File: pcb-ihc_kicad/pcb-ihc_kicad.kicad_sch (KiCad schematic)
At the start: 76 parts, among them J1 D-IN with pullup, J10 D-IN with pulldown, J11 2x N-Mosfet, J2 Screw_Terminal_01x01, J3 Screw_Terminal_01x01, J4 Screw_Terminal_01x01, J5 Screw_Terminal_01x01, J6 Screw_Terminal_01x01, J7 Screw_Terminal_01x01, J8 Screw_Terminal_01x01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

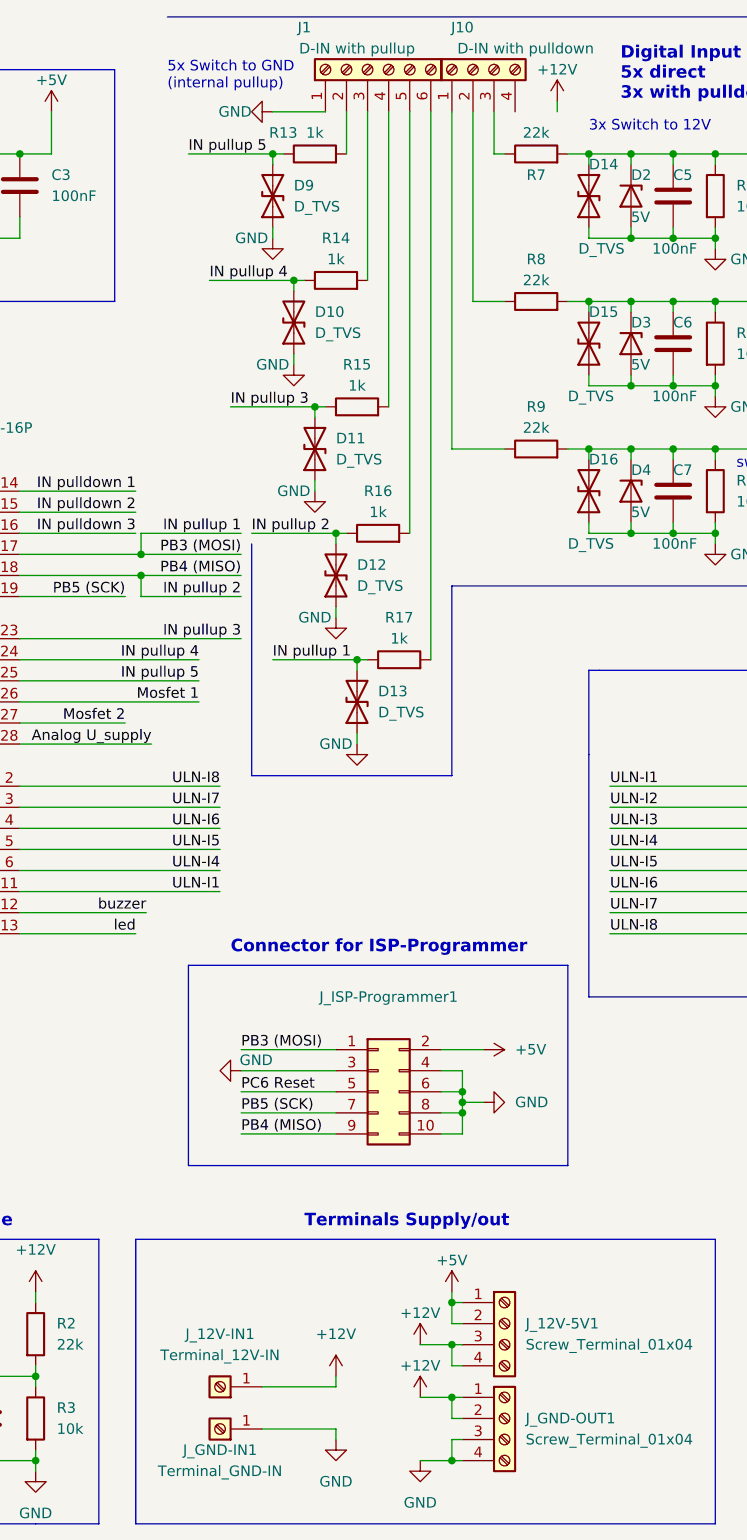
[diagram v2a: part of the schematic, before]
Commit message: Optimize routing and layout
- fix track width on several locations (1.5 to 2mm)
- minor changes in routing
- move relays closer together
- add additional 12V input terminal
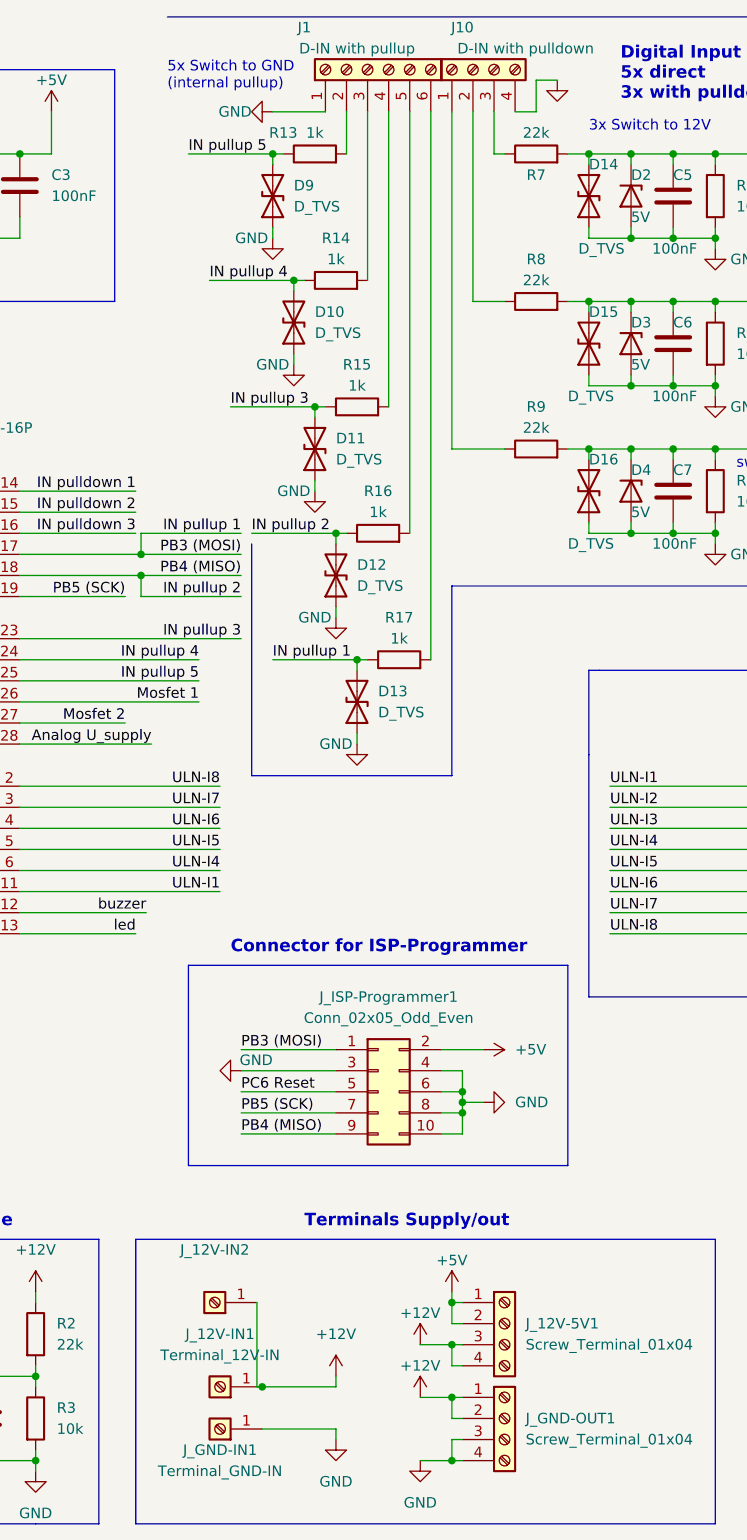
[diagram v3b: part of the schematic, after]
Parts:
- added J_12V-IN2: (no value), custom_footprints:my_KlemmeWago2604-single, symbol Connector:Screw_Terminal_01x01
- J_ISP-Programmer1: value (none) -> Conn_02x05_Odd_Even; footprint (none) -> custom_footprints:my_wannenstecker_2x5
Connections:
- net +12V: now also J_12V-IN2.1 (Pin_1)
- net GND: now also J10.4 (Pin_4)
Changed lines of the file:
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@@
   (junction (at 161.29 76.2) (diameter 0) (color 0 0 0 0)
   )
+  (junction (at 116.84 179.07) (diameter 0) (color 0 0 0 0)
+  )
   (junction (at 171.45 76.2) (diameter 0) (color 0 0 0 0)
   )
@@
     (stroke (width 0) (type default) (color 0 0 0 0))
   )
+  (wire (pts (xy 149.86 25.4) (xy 147.32 25.4))
+    (stroke (width 0) (type default) (color 0 0 0 0))
+  )
   (wire (pts (xy 208.28 90.17) (xy 208.28 114.3))
     (stroke (width 0) (type default) (color 0 0 0 0))
@@
     (stroke (width 0) (type default) (color 0 0 0 0))
   )
+  (wire (pts (xy 116.205 179.07) (xy 116.84 179.07))
+    (stroke (width 0) (type default) (color 0 0 0 0))
+  )
   (wire (pts (xy 166.37 40.64) (xy 171.45 40.64))
     (stroke (width 0) (type default) (color 0 0 0 0))
@@
     (stroke (width 0) (type default) (color 0 0 0 0))
   )
+  (wire (pts (xy 152.4 21.59) (xy 149.86 21.59))
+    (stroke (width 0) (type default) (color 0 0 0 0))
+  )
   (wire (pts (xy 74.295 187.96) (xy 83.185 187.96))
     (stroke (width 0) (type default) (color 0 0 0 0))
@@
     (stroke (width 0) (type default) (color 0 0 0 0))
   )
-  (wire (pts (xy 76.2 40.64) (xy 76.2 41.91))
+  (wire (pts (xy 149.86 21.59) (xy 149.86 25.4))
     (stroke (width 0) (type default) (color 0 0 0 0))
   )
-  (wire (pts (xy 152.4 24.13) (xy 152.4 25.4))
+  (wire (pts (xy 76.2 40.64) (xy 76.2 41.91))
     (stroke (width 0) (type default) (color 0 0 0 0))
   )
@@
     (stroke (width 0) (type default) (color 0 0 0 0))
   )
+  (wire (pts (xy 116.205 168.91) (xy 116.205 179.07))
+    (stroke (width 0) (type default) (color 0 0 0 0))
+  )
   (wire (pts (xy 52.07 40.64) (xy 62.23 40.64))
     (stroke (width 0) (type default) (color 0 0 0 0))
@@
     (pin "1")
   )
-  (symbol (lib_id "power:+12V") (at 152.4 24.13 0) (unit 1)
-    (in_bom yes) (on_board yes)
-    (property "Reference" "#PWR0148" (id 0) (at 152.4 27.94 0)
-      (effects (font (size 1.27 1.27)) hide)
-    )
-    (property "Value" "+12V" (id 1) (at 152.4 20.32 0))
-    (property "Footprint" "" (id 2) (at 152.4 24.13 0)
-      (effects (font (size 1.27 1.27)) hide)
-    )
-    (property "Datasheet" "" (id 3) (at 152.4 24.13 0)
-      (effects (font (size 1.27 1.27)) hide)
-    )
-    (pin "1")
-  )
   (symbol (lib_id "Connector:Screw_Terminal_01x01") (at 256.54 128.27 0) (unit 1)
     (in_bom yes) (on_board yes) (fields_autoplaced)
@@
     (pin "4")
   )
+  (symbol (lib_id "power:GND") (at 152.4 21.59 0) (unit 1)
+    (in_bom yes) (on_board yes)
+    (property "Reference" "#PWR?" (id 0) (at 152.4 27.94 0)
+      (effects (font (size 1.27 1.27)) hide)
+    )
+    (property "Value" "" (id 1) (at 153.035 25.4 0))
+    (property "Footprint" "" (id 2) (at 152.4 21.59 0)
+      (effects (font (size 1.27 1.27)) hide)
+    )
+    (property "Datasheet" "" (id 3) (at 152.4 21.59 0)
+      (effects (font (size 1.27 1.27)) hide)
+    )
+    (pin "1")
+  )
   (symbol (lib_id "Device:LED") (at 41.91 104.14 180) (unit 1)
     (in_bom yes) (on_board yes)
@@
     (pin "2")
   )
+  (symbol (lib_id "Connector:Screw_Terminal_01x01") (at 111.125 168.91 180) (unit 1)
+    (in_bom yes) (on_board yes) (fields_autoplaced)
+    (property "Reference" "J_12V-IN2" (id 0) (at 111.125 162.56 0))
+    (property "Value" "" (id 1) (at 111.125 165.1 0))
+    (property "Footprint" "custom_footprints:my_KlemmeWago2604-single" (id 2) (at 111.125 168.91 0)
+      (effects (font (size 1.27 1.27)) hide)
+    )
+    (property "Datasheet" "~" (id 3) (at 111.125 168.91 0)
+      (effects (font (size 1.27 1.27)) hide)
+    )
+    (pin "1")
+  )
   (symbol (lib_id "power:+12V") (at 236.22 143.51 270) (unit 1)
     (in_bom yes) (on_board yes) (fields_autoplaced)
@@
     (in_bom yes) (on_board yes) (fields_autoplaced)
     (property "Reference" "J_ISP-Programmer1" (id 0) (at 132.08 132.08 0))
-    (property "Value" "" (id 1) (at 132.08 134.62 0))
-    (property "Footprint" "" (id 2) (at 130.81 143.51 0)
+    (property "Value" "Conn_02x05_Odd_Even" (id 1) (at 132.08 134.62 0))
+    (property "Footprint" "custom_footprints:my_wannenstecker_2x5" (id 2) (at 130.81 143.51 0)
       (effects (font (size 1.27 1.27)) hide)
     )
@@
       (reference "#PWR0147") (unit 1) (value "GND") (footprint "")
     )
-    (path "/1c4456e1-5e0f-4596-b426-054b5a39fdc1"
-      (reference "#PWR0148") (unit 1) (value "+12V") (footprint "")
-    )
     (path "/ffe15c22-6549-4880-ae32-c2e96a1323c9"
       (reference "#PWR0149") (unit 1) (value "GND") (footprint "")
@@
       (reference "#PWR0152") (unit 1) (value "+12V") (footprint "")
     )
+    (path "/1ede0768-e859-4316-8ade-3fe07133097f"
+      (reference "#PWR?") (unit 1) (value "GND") (footprint "")
+    )
     (path "/4f7b24c2-4bfe-4f23-a154-b1059c420795"
       (reference "BZ1") (unit 1) (value "Buzzer") (footprint "Buzzer_Beeper:Buzzer_12x9.5RM7.6")
@@
       (reference "J_12V-IN1") (unit 1) (value "Terminal_12V-IN") (footprint "custom_footprints:my_KlemmeWago2604-single")
     )
+    (path "/4888375b-5458-4871-a1fa-505252626301"
+      (reference "J_12V-IN2") (unit 1) (value "Terminal_12V-IN-support") (footprint "custom_footprints:my_KlemmeWago2604-single")
+    )
     (path "/71d4b6af-077c-43c1-acb9-a17c885be490"

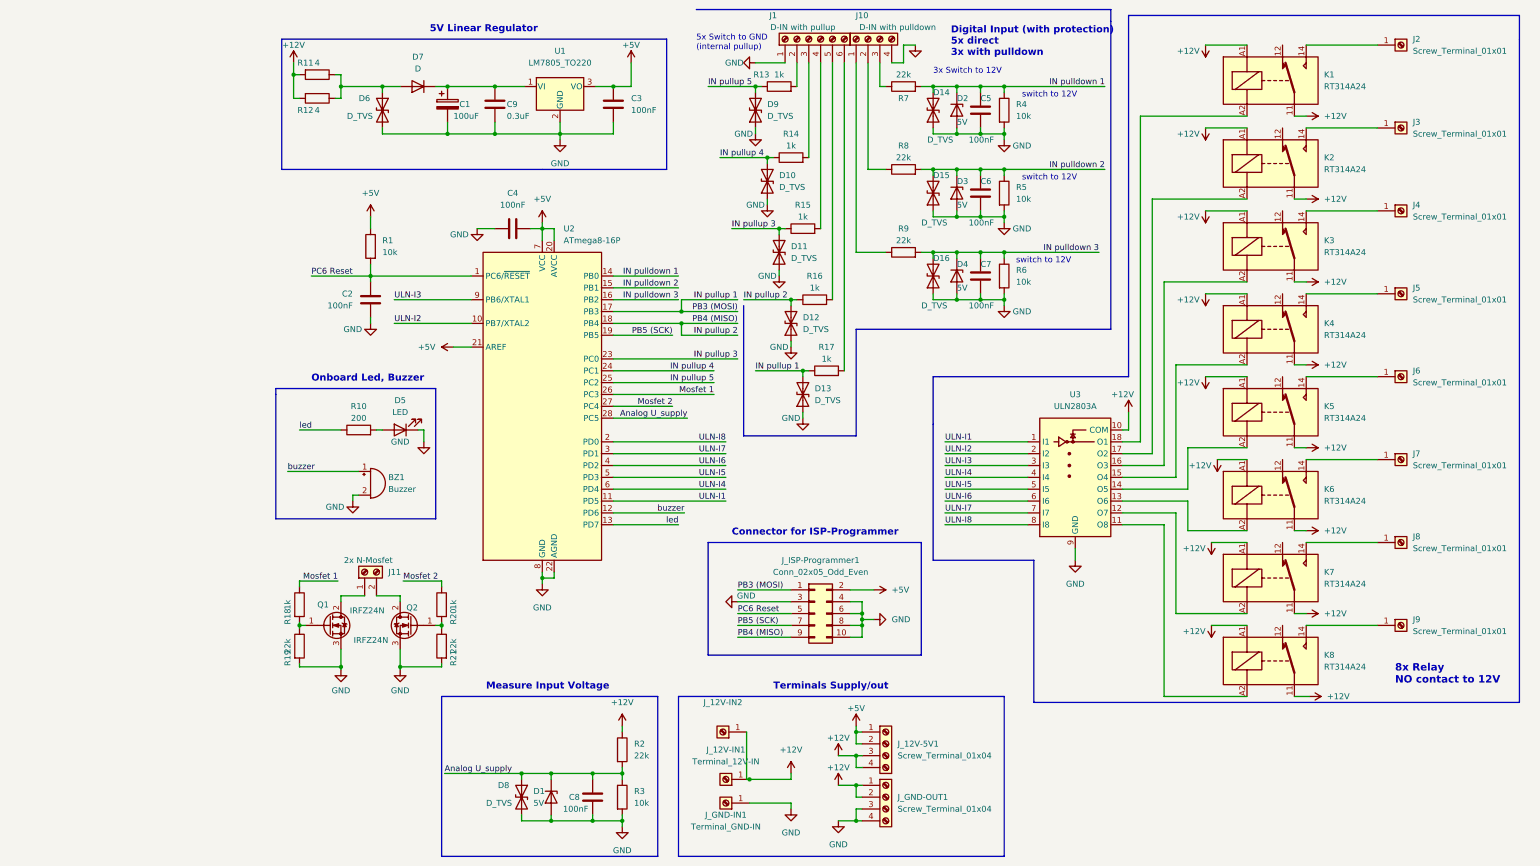
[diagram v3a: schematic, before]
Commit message: Add terminal descriptions, Clean up schematic
- Add detailed terminal/connector descriptions (e.g. which uC pin)
- Positioned labels in layout outside of pcb
- cleanup in schematic reorder groups, fix boxes...
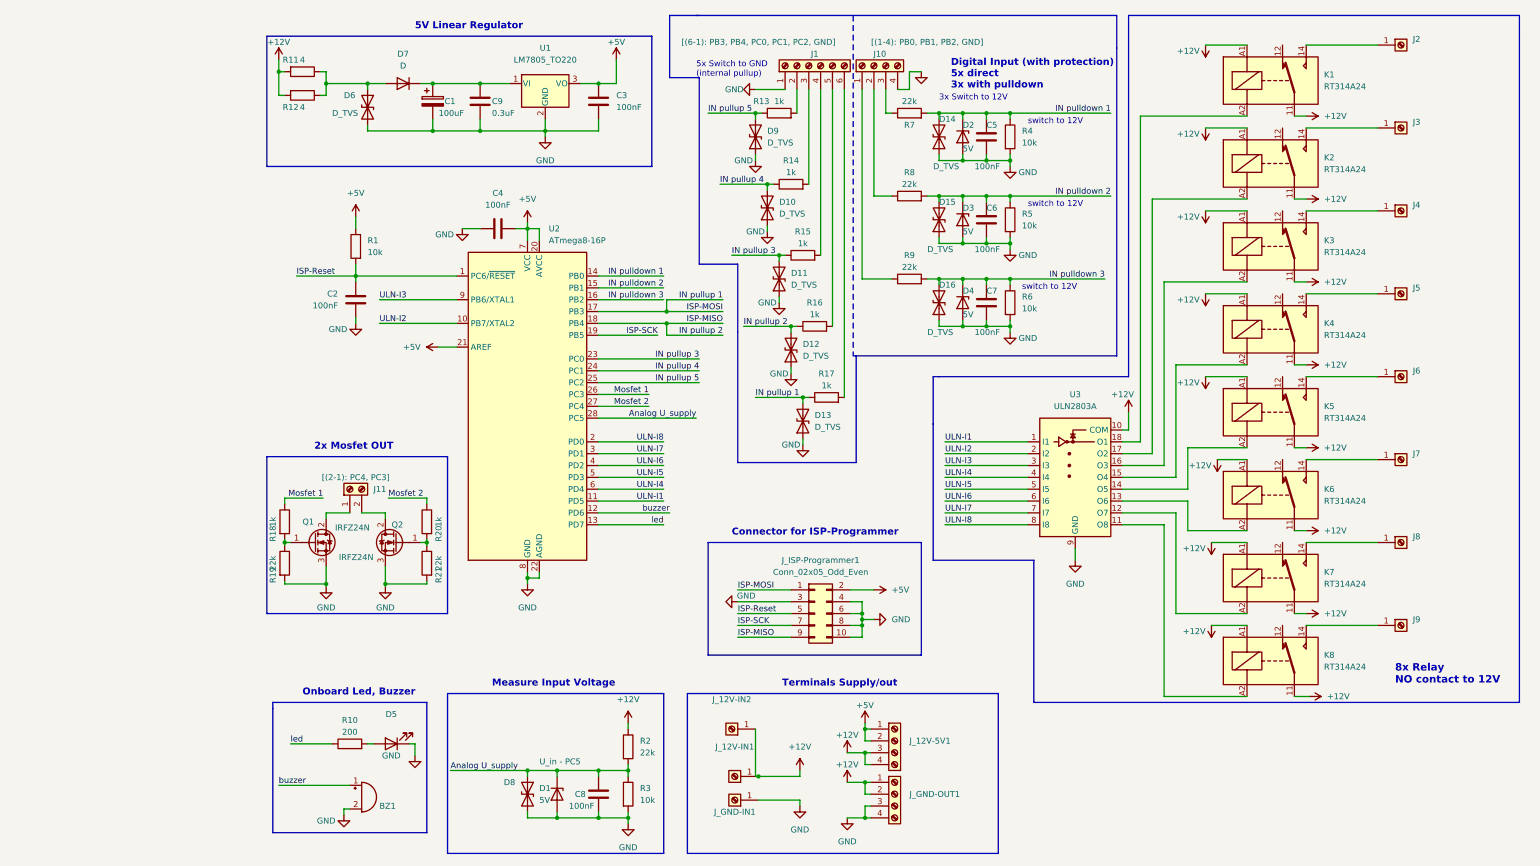
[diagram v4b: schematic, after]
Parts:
- BZ1: value Buzzer -> (none)
- D5: value LED -> (none)
- D8: value D_TVS -> (none); footprint custom_footprints:my_D10_11 -> (none); Desc (none) -> U_in - PC5
- J1: value D-IN with pullup -> (none); footprint TerminalBlock_WAGO:TerminalBlock_WAGO_236-406_1x06_P5.00mm_45Degree -> (none); Desc (none) -> [(6-1): PB3, PB4, PC0, PC1, PC2, GND]
- J10: value D-IN with pulldown -> (none); footprint TerminalBlock_WAGO:TerminalBlock_WAGO_236-404_1x04_P5.00mm_45Degree -> (none); Desc (none) -> [(1-4): PB0, PB1, PB2, GND]
- J11: value 2x N-Mosfet -> (none); footprint TerminalBlock_WAGO:TerminalBlock_WAGO_236-402_1x02_P5.00mm_45Degree -> (none); Desc (none) -> [(2-1): PC4, PC3]
- J2, J3, J4, J5, J6, J7, J8, J9: value Screw_Terminal_01x01 -> (none)
- J_12V-5V1, J_GND-OUT1: value Screw_Terminal_01x04 -> (none)
- J_12V-IN1: value Terminal_12V-IN -> (none)
- J_GND-IN1: value Terminal_GND-IN -> (none)
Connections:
- net PB5 (SCK) renamed ISP-SCK
- net PC6 Reset renamed ISP-Reset
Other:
- note added: "2x Mosfet OUT"
- moved on the sheet: BZ1, C1, C2, C3, C4, C5, C6, C7, C8, C9, D1, D10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
